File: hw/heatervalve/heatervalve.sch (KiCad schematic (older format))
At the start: 9 parts

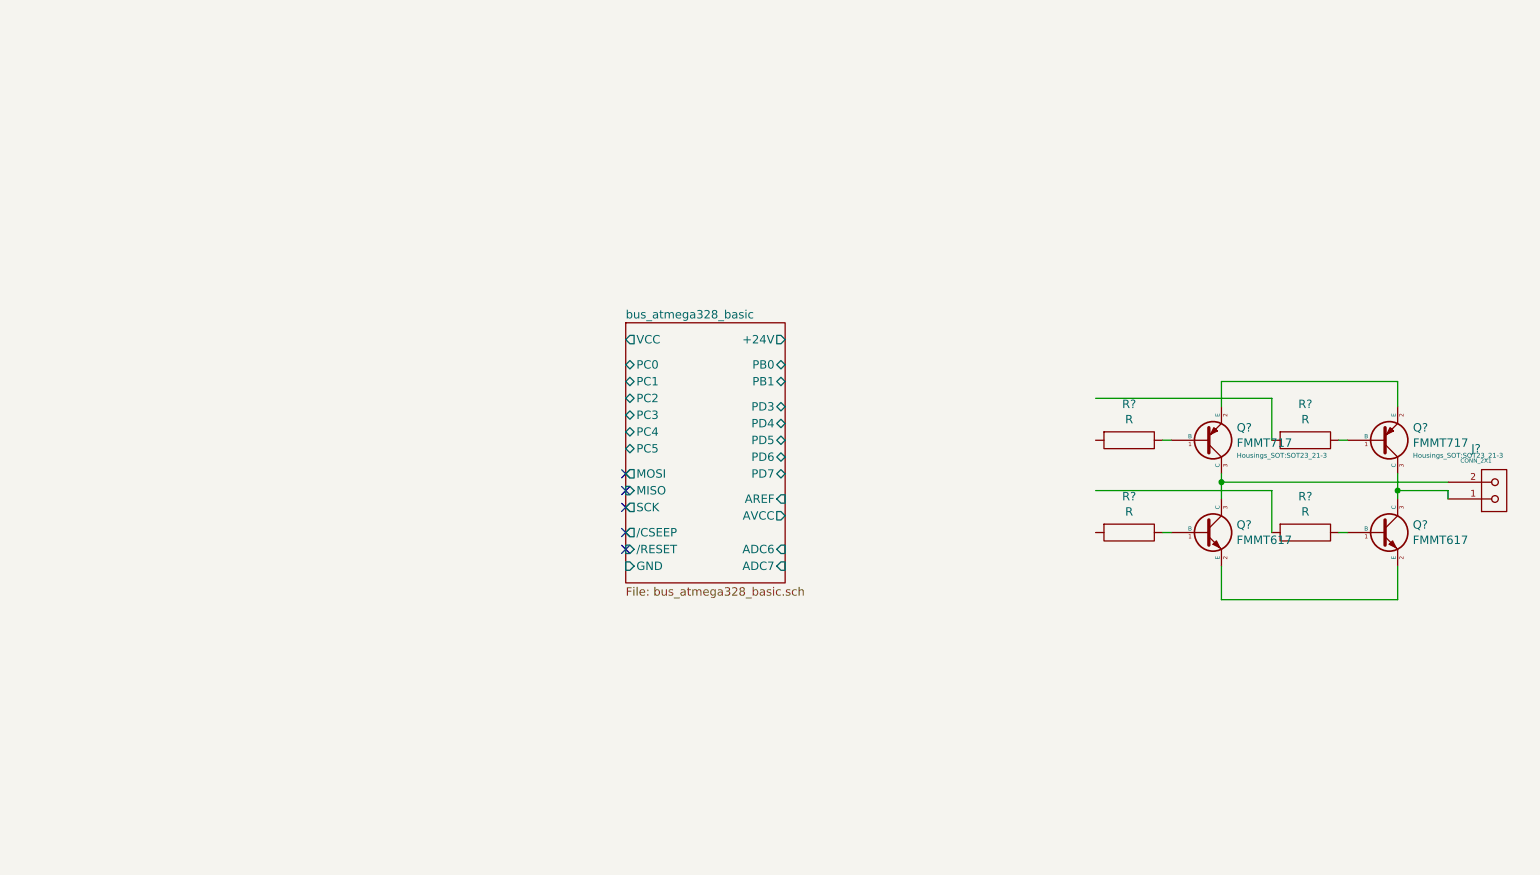
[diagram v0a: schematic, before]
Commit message: first complete draft of heatervalve schematic
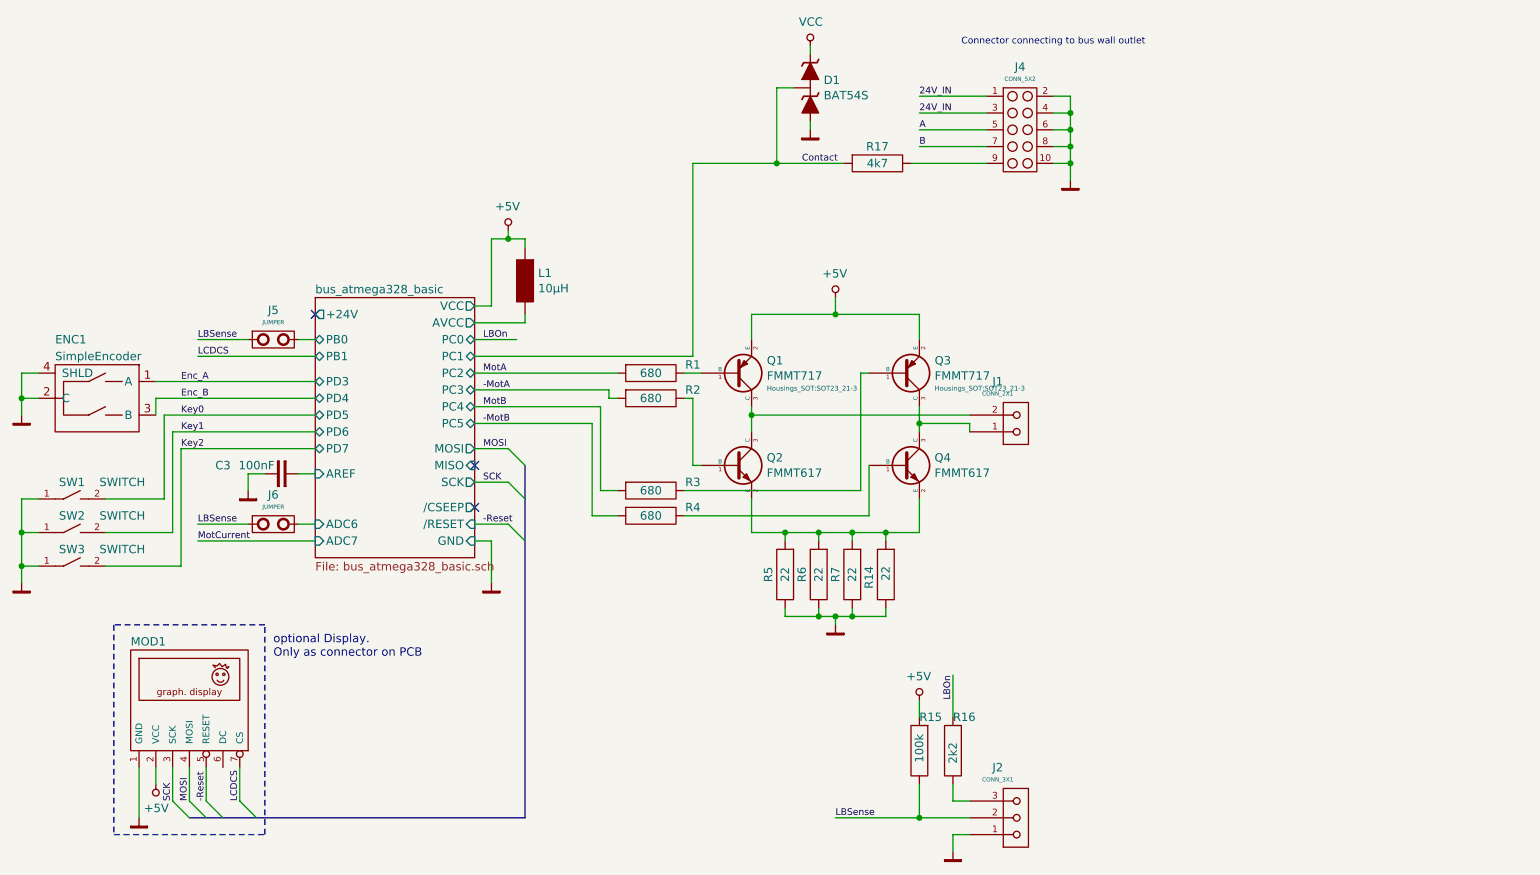
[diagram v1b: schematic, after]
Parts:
- added C3: 100nF, Capacitors_SMD:C_0805, symbol standard:C
- added D1: BAT54S, Diode_SMD:D_SOD323, symbol diodes:BAT54S
- added ENC1: SimpleEncoder, Switch_Encoder:EncodeNonameHeatervalve, symbol encoder:SimpleEncoder
- added J2: CONN_3X1, Connector_Header:HEADER_3x1, symbol connectors:CONN_3X1
- added J4: CONN_5X2, Connector_Header:HEADER_5x2, symbol connectors:CONN_5X2
- added J5, J6: JUMPER, Resistor:R_0805, symbol connectors:JUMPER
- added L1: 10µH, Inductor:L_0805, symbol standard:L
- added MOD1: Graphic-OLED-Display_4wireSPI, Connector_Header:HEADER_7x1, symbol display:Graphic-OLED-Display_4wireSPI
- added R14, R5, R6, R7: 22, Resistor:R_0805, symbol standard:R
- added R15: 100k, Resistor:R_0805, symbol standard:R
- added R16: 2k2, Resistor:R_0805, symbol standard:R
- added R17: 4k7, Resistor:R_0805, symbol standard:R
- added SW1, SW2, SW3: SWITCH, Switch_Miscelleaneus:PushButton_SPST_THT_5x5mm, symbol standard:SWITCH
- J1: renamed from J?; footprint (none) -> Connector_Header:HEADER_2x1
- R1, R2, R3, R4: renamed from R?; value R -> 680; footprint (none) -> Resistor:R_0805
- gave numbers to parts that had none: 4
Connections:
- net labels added: +5V, -MotA, -MotB, -Reset, 24V_IN, A, B, Contact, Enc_A, Enc_B, GND, Key0, Key1, Key2, LBOn, LBSense, LCDCS, MOSI, MotA, MotB, MotCurrent, SCK, VCC
- wire segments 21 -> 134
- no-connect marks 5 -> 3
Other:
- note added: "Connector connecting to bus wall outlet"
- note added: "optional Display.\nOnly as connector on PCB"
- moved on the sheet: J1, Q1, Q2, Q3, Q4, R1, R2, R3, R4

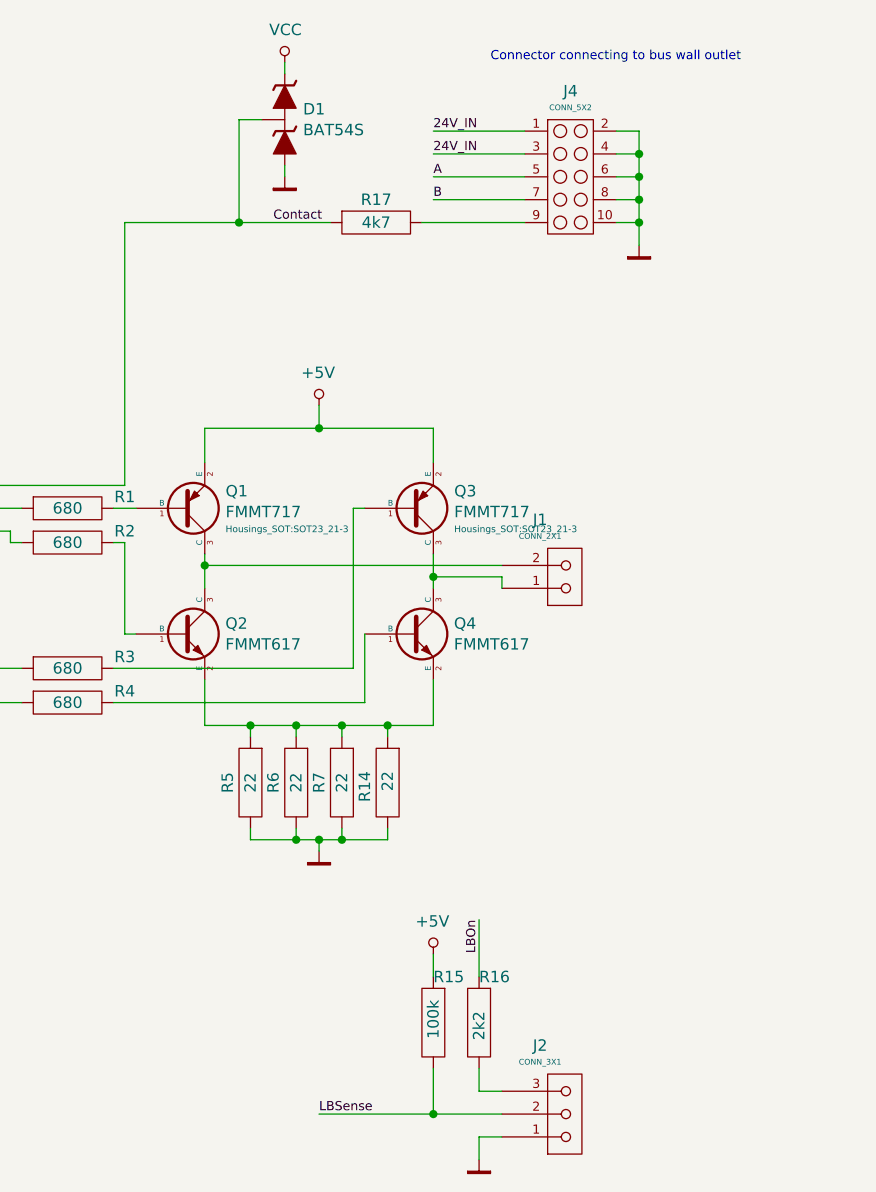
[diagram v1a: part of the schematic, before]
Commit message: Add heatervalve schematic
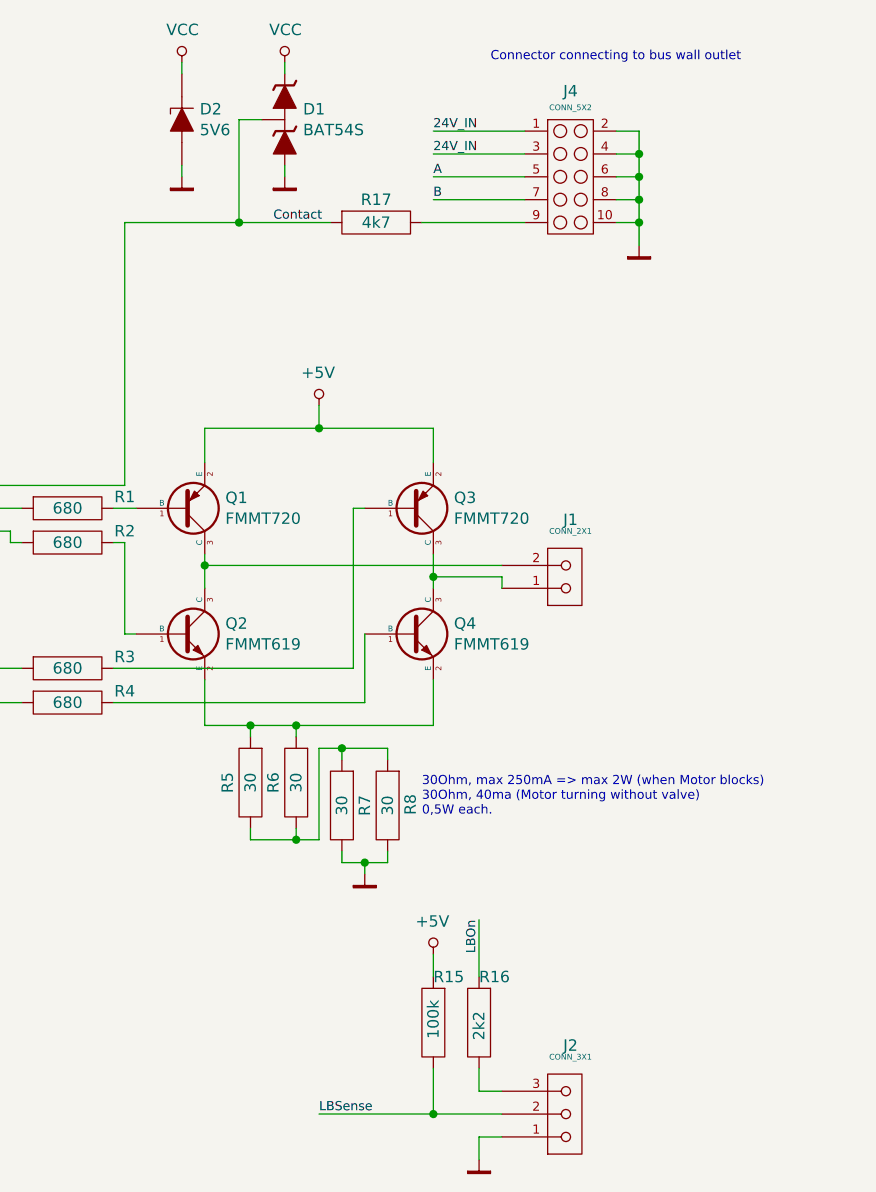
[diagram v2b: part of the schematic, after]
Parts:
- removed Q1, Q3: FMMT717, Housings_SOT:SOT23_21-3, symbol transistors:FMMT717
- removed Q2, Q4: FMMT617, Housings_SOT:SOT23_21-3, symbol transistors:FMMT617
- added D2: 5V6, Diode_SMD:D_MINIMELF, symbol standard:ZD
- added Q1, Q3: FMMT720, Housings_SOT:SOT23_21-3, symbol transistors:FMMT720
- added Q2, Q4: FMMT619, Housings_SOT:SOT23_21-3, symbol transistors:FMMT619
- R5, R6, R7: value 22 -> 30; footprint Resistor:R_0805 -> Resistor:R_1206
- R8: renamed from R14; value 22 -> 30; footprint Resistor:R_0805 -> Resistor:R_1206
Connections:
- net +5V: now also Q1.2 (E), Q3.2 (E)
- net GND: now also D2.1 (A); no longer R5.2, R6.2
- net VCC: now also D2.2 (C)
- net at R2.2: now also Q2.1 (B)
- net at R5.1, R6.1: now also Q2.2 (E), Q4.2 (E); no longer R7.1, R8.1
- net at J1.2: now also Q1.3 (C), Q2.3 (C)
- net at R4.2: now also Q4.1 (B)
- net at J1.1: now also Q3.3 (C), Q4.3 (C)
- net at R1.2: now also Q1.1 (B)
- net at R3.2: now also Q3.1 (B)
- new net: R5.2, R6.2, R7.1, R8.1
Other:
- note added: "30Ohm, max 250mA => max 2W (when Motor blocks)\n30Ohm, 40ma (Motor turning without valve)\n0,5W each.\n"
- moved on the sheet: R7, R8
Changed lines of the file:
@@
 Sheet 1 2
 Title "heatervalve"
-Date "2022-02-20"
+Date "2022-02-28"
 Rev "1"
 Comp "KoeWiBa"
@@
 Comment4 ""
 $EndDescr
-$Comp
-L transistors:FMMT617 Q2
-U 1 1 61E3E4AE
-P 6100 3600
-F 0 "Q2" H 6290 3646 50  0000 L CNN
-F 1 "FMMT617" H 6290 3555 50  0000 L CNN
-F 2 "Housings_SOT:SOT23_21-3" H 6000 3702 29  0001 C CNN
-F 3 "" H 6100 3600 60  0000 C CNN
-	1    6100 3600
-	1    0    0    -1
-$EndComp
-$Comp
-L transistors:FMMT617 Q4
-U 1 1 61E3EA00
-P 7100 3600
-F 0 "Q4" H 7290 3646 50  0000 L CNN
-F 1 "FMMT617" H 7290 3555 50  0000 L CNN
-F 2 "Housings_SOT:SOT23_21-3" H 7000 3702 29  0001 C CNN
-F 3 "" H 7100 3600 60  0000 C CNN
-	1    7100 3600
-	1    0    0    -1
-$EndComp
-$Comp
-L transistors:FMMT717 Q1
-U 1 1 61E3F6D2
-P 6100 3050
-F 0 "Q1" H 6291 2975 50  0000 L CNN
-F 1 "FMMT717" H 6291 3066 50  0000 L CNN
-F 2 "Housings_SOT:SOT23_21-3" H 6291 3141 29  0000 L CNN
-F 3 "" H 6100 3050 60  0000 C CNN
-	1    6100 3050
-	1    0    0    1
-$EndComp
-$Comp
-L transistors:FMMT717 Q3
-U 1 1 61E3FCD8
-P 7100 3050
-F 0 "Q3" H 7291 2975 50  0000 L CNN
-F 1 "FMMT717" H 7291 3066 50  0000 L CNN
-F 2 "Housings_SOT:SOT23_21-3" H 7291 3141 29  0000 L CNN
-F 3 "" H 7100 3050 60  0000 C CNN
-	1    7100 3050
-	1    0    0    1
-$EndComp
 Wire Wire Line
 	6200 2850 6200 2700
@@
 U 1 1 61E41AF2
 P 7700 3350
-F 0 "J1" H 7667 3100 50  0000 C CNN
-F 1 "CONN_2X1" H 7667 3172 25  0000 C CNN
+F 0 "J1" H 7800 3100 50  0000 C CNN
+F 1 "CONN_2X1" H 7800 3150 25  0000 C CNN
 F 2 "Connector_Header:HEADER_2x1" H 7700 3350 60  0001 C CNN
 F 3 "" H 7700 3350 60  0000 C CNN
@@
 L power:GND #PWR08
 U 1 1 62039745
-P 6700 4550
-F 0 "#PWR08" H 6700 4350 50  0001 C CNN
-F 1 "GND" H 6700 4440 50  0001 C CNN
-F 2 "" H 6700 4550 50  0001 C CNN
-F 3 "" H 6700 4550 50  0001 C CNN
-	1    6700 4550
+P 6900 4650
+F 0 "#PWR08" H 6900 4450 50  0001 C CNN
+F 1 "GND" H 6900 4540 50  0001 C CNN
+F 2 "" H 6900 4650 50  0001 C CNN
+F 3 "" H 6900 4650 50  0001 C CNN
+	1    6900 4650
 	1    0    0    -1
 $EndComp
@@
 P 6600 4250
 F 0 "R6" H 6600 4150 50  0000 C CNN
-F 1 "22" H 6600 4250 50  0000 C CNN
-F 2 "Resistor:R_0805" H 6600 4250 60  0001 C CNN
+F 1 "30" H 6600 4250 50  0000 C CNN
+F 2 "Resistor:R_1206" H 6600 4250 60  0001 C CNN
 F 3 "" H 6600 4250 60  0000 C CNN
 	1    6600 4250
@@
 P 6400 4250
 F 0 "R5" H 6400 4150 50  0000 C CNN
-F 1 "22" H 6400 4250 50  0000 C CNN
-F 2 "Resistor:R_0805" H 6400 4250 60  0001 C CNN
+F 1 "30" H 6400 4250 50  0000 C CNN
+F 2 "Resistor:R_1206" H 6400 4250 60  0001 C CNN
 F 3 "" H 6400 4250 60  0000 C CNN
 	1    6400 4250
@@
 U 1 1 620BDEE2
 P 7700 5700
-F 0 "J2" H 7667 5400 50  0000 C CNN
-F 1 "CONN_3X1" H 7667 5472 25  0000 C CNN
+F 0 "J2" H 7800 5400 50  0000 C CNN
+F 1 "CONN_3X1" H 7800 5450 25  0000 C CNN
 F 2 "Connector_Header:HEADER_3x1" H 7700 5700 60  0001 C CNN
 F 3 "" H 7700 5700 60  0000 C CNN
@@
 L standard:R R7
 U 1 1 6205C5EB
-P 6800 4250
-F 0 "R7" H 6800 4150 50  0000 C CNN
-F 1 "22" H 6800 4250 50  0000 C CNN
-F 2 "Resistor:R_0805" H 6800 4250 60  0001 C CNN
-F 3 "" H 6800 4250 60  0000 C CNN
-	1    6800 4250
+P 6800 4350
+F 0 "R7" H 6800 4450 50  0000 C CNN
+F 1 "30" H 6800 4350 50  0000 C CNN
+F 2 "Resistor:R_1206" H 6800 4350 60  0001 C CNN
+F 3 "" H 6800 4350 60  0000 C CNN
+	1    6800 4350
 	0    1    1    0
 $EndComp
 $Comp
-L standard:R R14
+L standard:R R8
 U 1 1 621371F6
-P 7000 4250
-F 0 "R14" H 6950 4150 50  0000 L CNN
-F 1 "22" H 6950 4250 50  0000 L CNN
-F 2 "Resistor:R_0805" H 7000 4250 60  0001 C CNN
-F 3 "" H 7000 4250 60  0000 C CNN
-	1    7000 4250
+P 7000 4350
+F 0 "R8" H 6950 4450 50  0000 L CNN
+F 1 "30" H 7000 4350 50  0000 C CNN
+F 2 "Resistor:R_1206" H 7000 4350 60  0001 C CNN
+F 3 "" H 7000 4350 60  0000 C CNN
+	1    7000 4350
 	0    1    1    0
 $EndComp
@@
 Connection ~ 6600 4000
 Wire Wire Line
-	6600 4000 6800 4000
-Wire Wire Line
-	6800 4050 6800 4000
-Connection ~ 6800 4000
-Wire Wire Line
-	6800 4000 7000 4000
-Wire Wire Line
-	7000 4050 7000 4000
-Connection ~ 7000 4000
-Wire Wire Line
-	7000 4000 7200 4000
-Wire Wire Line
-	7000 4450 7000 4500
-Wire Wire Line
-	7000 4500 6800 4500
-Wire Wire Line
 	6400 4500 6400 4450
 Wire Wire Line
 	6600 4450 6600 4500
+Wire Wire Line
+	6600 4500 6400 4500
+Text Notes 7150 4400 0    40   ~ 0
+30Ohm, max 250mA => max 2W (when Motor blocks)\n30Ohm, 40ma (Motor turning without valve)\n0,5W each.\n
+Wire Wire Line
+	6600 4000 7200 4000
+Wire Wire Line
+	6800 4150 6800 4100
+Wire Wire Line
+	6800 4100 7000 4100
+Wire Wire Line
+	7000 4100 7000 4150
+Wire Wire Line
+	6800 4100 6700 4100
+Wire Wire Line
+	6700 4100 6700 4500
+Wire Wire Line
+	6700 4500 6600 4500
+Connection ~ 6800 4100
 Connection ~ 6600 4500
 Wire Wire Line
-	6600 4500 6400 4500
-Wire Wire Line
-	6800 4450 6800 4500
-Connection ~ 6800 4500
-Wire Wire Line
-	6800 4500 6700 4500
-Wire Wire Line
-	6700 4500 6700 4550
+	6800 4550 6800 4600
+Wire Wire Line
+	6800 4600 6900 4600
+Wire Wire Line
+	7000 4600 7000 4550
+Wire Wire Line
+	6900 4650 6900 4600
+Connection ~ 6900 4600
+Wire Wire Line
+	6900 4600 7000 4600
+$Comp
+L standard:ZD D2
+U 1 1 62146ED5
+P 6100 1350
+F 0 "D2" V 6146 1272 50  0000 R CNN
+F 1 "5V6" V 6055 1272 50  0000 R CNN
+F 2 "Diode_SMD:D_MINIMELF" H 6100 1350 60  0001 C CNN
+F 3 "" H 6100 1350 60  0000 C CNN
+	1    6100 1350
+	0    -1   -1   0
+$EndComp
+$Comp
+L power:VCC #PWR011
+U 1 1 621495D6
+P 6100 1100
+F 0 "#PWR011" H 6100 1275 50  0001 C CNN
+F 1 "VCC" H 6103 1243 50  0000 C CNN
+F 2 "" H 6100 1100 40  0001 C CNN
+F 3 "" H 6100 1100 40  0001 C CNN
+	1    6100 1100
+	1    0    0    -1
+$EndComp
+$Comp
+L power:GND #PWR012
+U 1 1 62149E85
+P 6100 1600
+F 0 "#PWR012" H 6100 1400 50  0001 C CNN
+F 1 "GND" H 6100 1490 50  0001 C CNN
+F 2 "" H 6100 1600 40  0001 C CNN
+F 3 "" H 6100 1600 40  0001 C CNN
+	1    6100 1600
+	1    0    0    -1
+$EndComp
+Wire Wire Line
+	6100 1100 6100 1150
+Wire Wire Line
+	6100 1550 6100 1600
+$Comp
+L transistors:FMMT720 Q1
+U 1 1 621E16C8
+P 6100 3050
+F 0 "Q1" H 6290 3004 50  0000 L CNN
+F 1 "FMMT720" H 6290 3095 50  0000 L CNN
+F 2 "Housings_SOT:SOT23_21-3" H 6291 3141 29  0001 L CNN
+F 3 "" H 6100 3050 60  0000 C CNN
+	1    6100 3050
+	1    0    0    1
+$EndComp
+$Comp
+L transistors:FMMT720 Q3
+U 1 1 621ED987
+P 7100 3050
+F 0 "Q3" H 7290 3004 50  0000 L CNN
+F 1 "FMMT720" H 7290 3095 50  0000 L CNN
+F 2 "Housings_SOT:SOT23_21-3" H 7291 3141 29  0001 L CNN
+F 3 "" H 7100 3050 60  0001 C CNN
+	1    7100 3050
+	1    0    0    1
+$EndComp
 Wire Bus Line
 	4850 3600 4850 5700
 Wire Bus Line
 	2850 5700 4850 5700
-Connection ~ 6700 4500
-Wire Wire Line
-	6700 4500 6600 4500
+$Comp
+L transistors:FMMT619 Q2
+U 1 1 621FAE8D
+P 6100 3600
+F 0 "Q2" H 6290 3646 50  0000 L CNN
+F 1 "FMMT619" H 6290 3555 50  0000 L CNN
+F 2 "Housings_SOT:SOT23_21-3" H 6000 3702 29  0001 C CNN
+F 3 "" H 6100 3600 60  0000 C CNN
+	1    6100 3600
+	1    0    0    -1
+$EndComp
+$Comp
+L transistors:FMMT619 Q4
+U 1 1 621FEB0E
+P 7100 3600
+F 0 "Q4" H 7290 3646 50  0000 L CNN
+F 1 "FMMT619" H 7290 3555 50  0000 L CNN
+F 2 "Housings_SOT:SOT23_21-3" H 7000 3702 29  0001 C CNN
+F 3 "" H 7100 3600 60  0000 C CNN
+	1    7100 3600
+	1    0    0    -1
+$EndComp
 $EndSCHEMATC
